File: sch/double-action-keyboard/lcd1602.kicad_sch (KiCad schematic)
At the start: 16 parts, among them U2 AQM1602XA-RN-GBW, U3 AQM1602Y-NLW-FBW

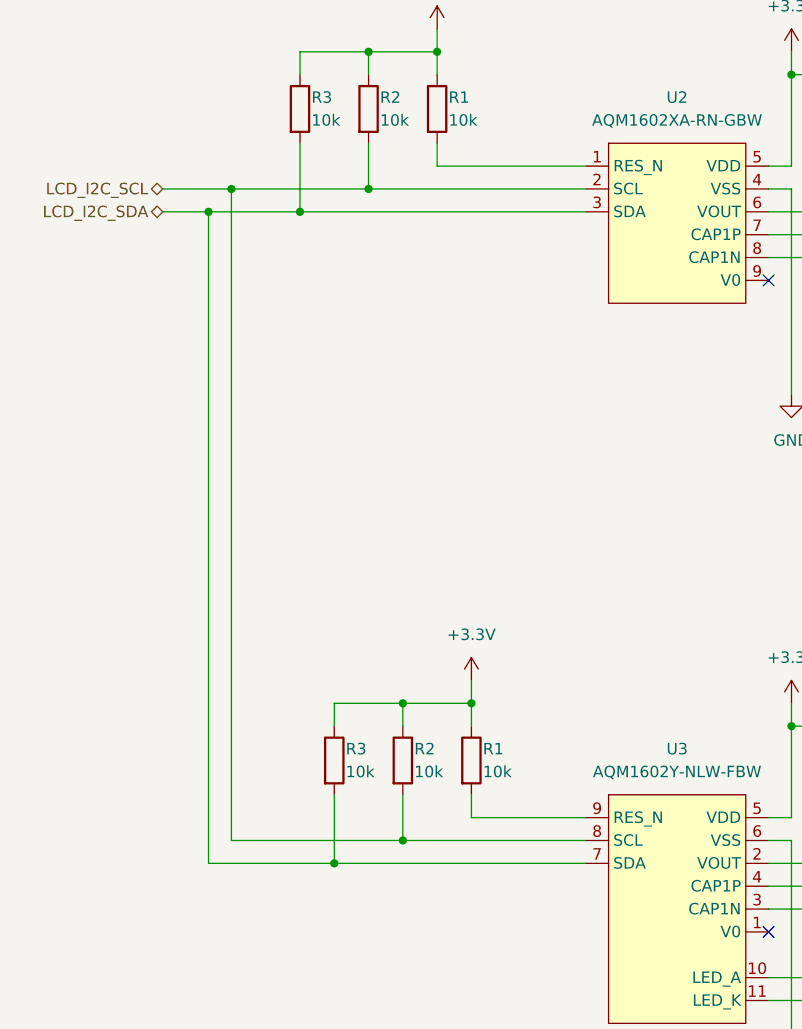
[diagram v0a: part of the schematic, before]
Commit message: ダイオードの配置と配線を行いました。
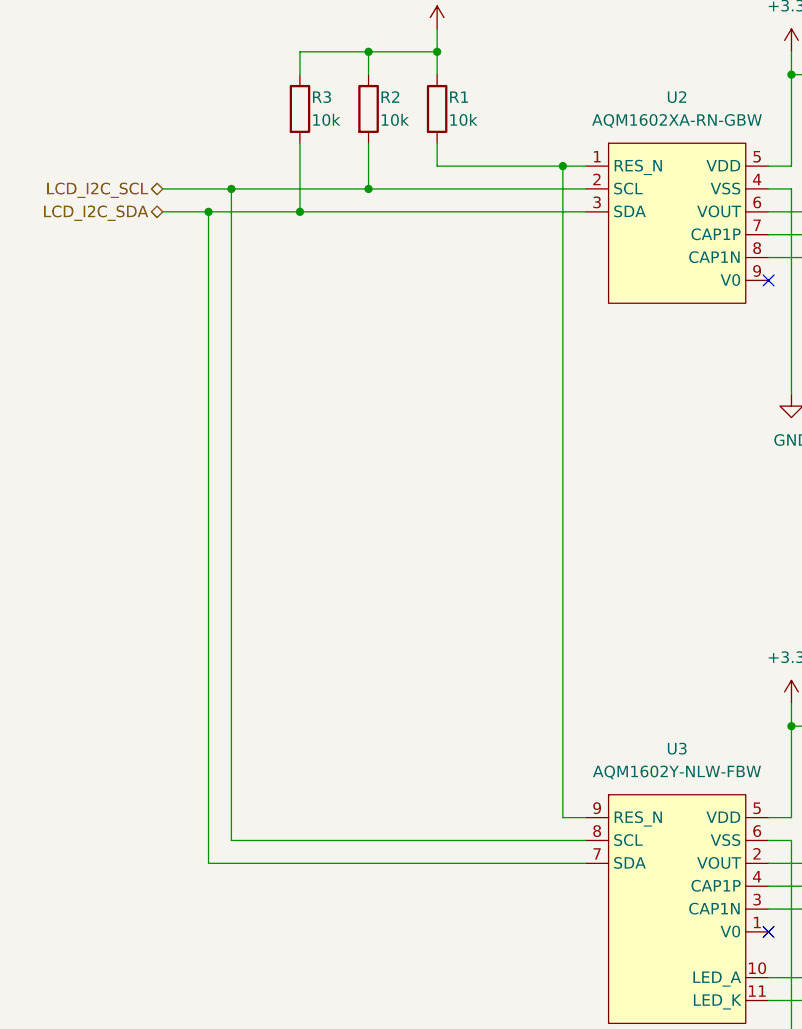
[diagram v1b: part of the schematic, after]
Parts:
- removed R1, R2, R3: 10k, Resistor_SMD:R_0603_1608Metric_Pad0.98x0.95mm_HandSolder, symbol Device:R
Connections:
- net at R1.2, U2.1 (RES_N): now also U3.9 (RES_N)

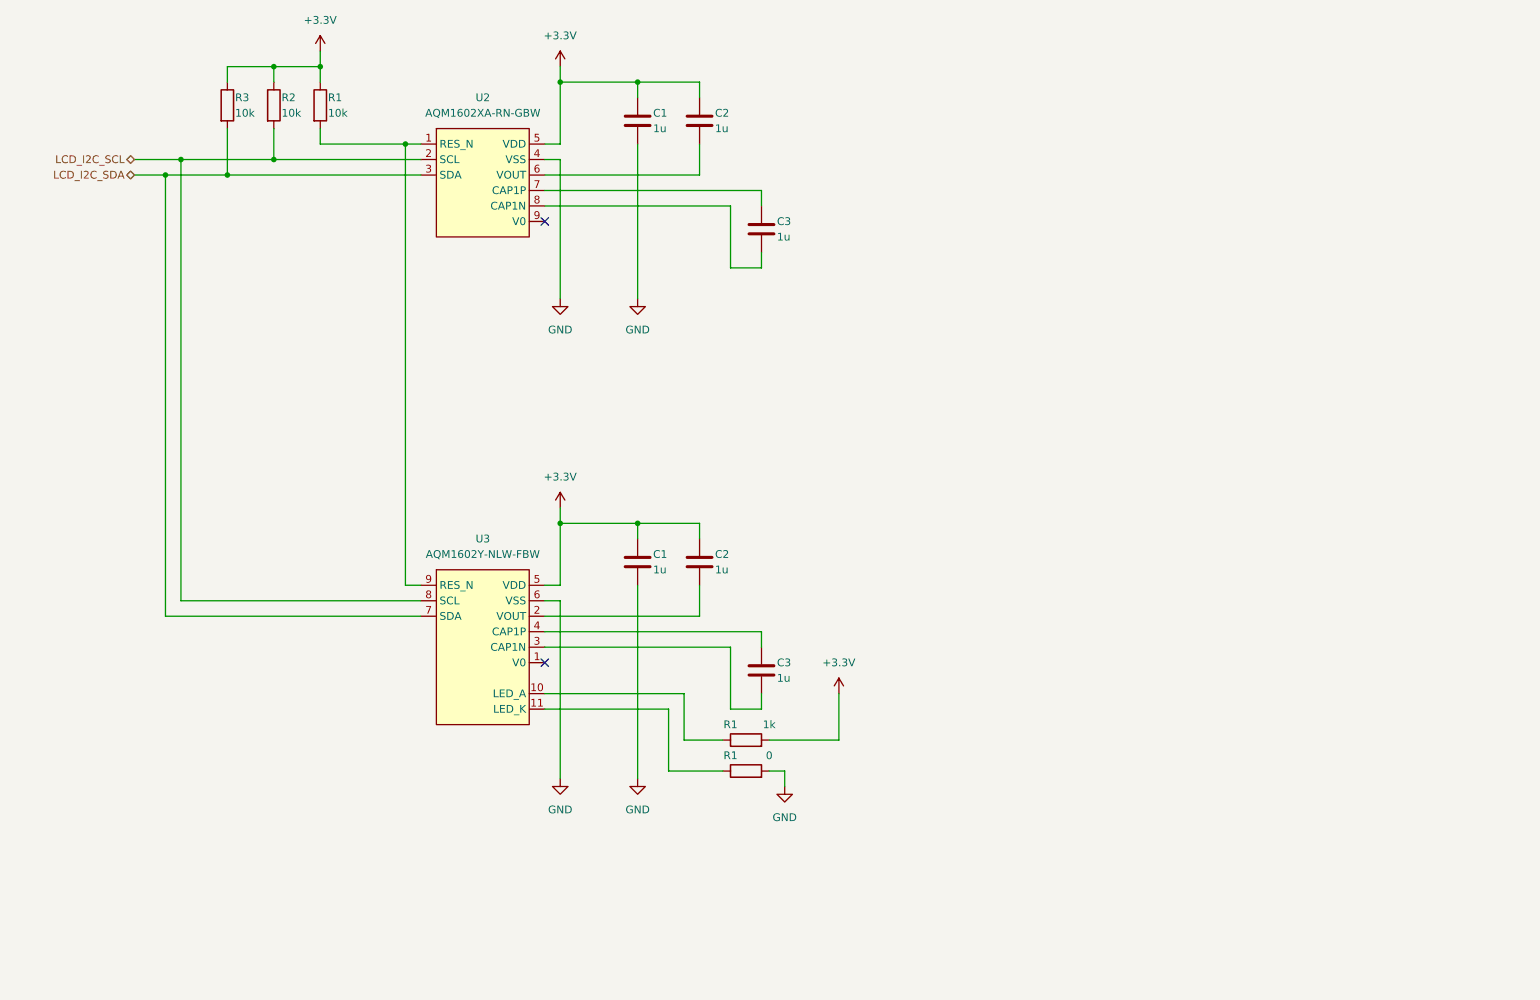
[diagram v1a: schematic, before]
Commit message: KiCad 8.0にアップデートしました。 部品配置をやり直し中。
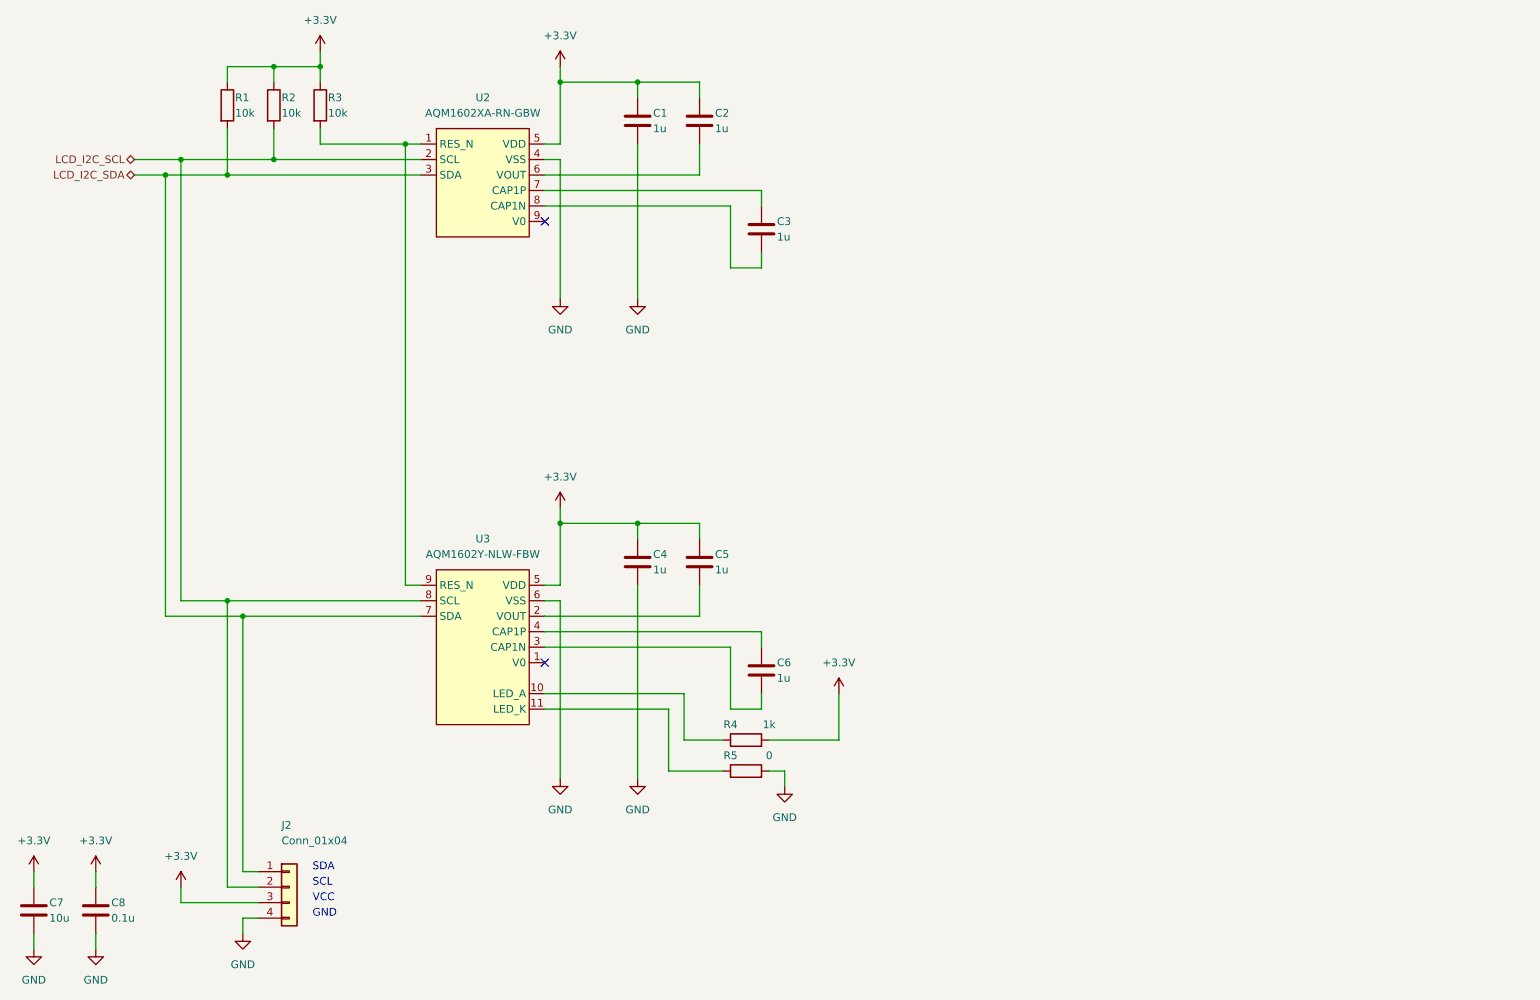
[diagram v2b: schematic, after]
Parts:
- added C7: 10u, Capacitor_SMD:C_0603_1608Metric_Pad1.08x0.95mm_HandSolder, symbol Device:C
- added C8: 0.1u, Capacitor_SMD:C_0603_1608Metric_Pad1.08x0.95mm_HandSolder, symbol Device:C
- added J2: Conn_01x04, Connector_PinHeader_2.54mm:PinHeader_1x04_P2.54mm_Vertical, symbol Connector_Generic:Conn_01x04
- renumbered C1 to C4, C2 to C5, C3 to C6, R3 to R1, R1 to R3, R1 to R4, R1 to R5
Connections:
- net +3.3V: now also C7.1, C8.1, J2.3 (Pin_3)
- net GND: now also C7.2, C8.2, J2.4 (Pin_4)
- net LCD_I2C_SCL: now also J2.2 (Pin_2)
- net LCD_I2C_SDA: now also J2.1 (Pin_1)
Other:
- note added: "GND"
- note added: "SCL"
- note added: "SDA"
- note added: "VCC"

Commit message: ざっくり配線しました。 線間はもっと詰める予定。
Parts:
- added C10: 0.1u, Capacitor_SMD:C_0603_1608Metric_Pad1.08x0.95mm_HandSolder, symbol Device:C
- added C9: 10u, Capacitor_SMD:C_0603_1608Metric_Pad1.08x0.95mm_HandSolder, symbol Device:C
- added J3: Conn_01x04, Connector_PinHeader_2.54mm:PinHeader_1x04_P2.54mm_Vertical, symbol Connector_Generic:Conn_01x04
- added R6: 10k, Resistor_SMD:R_0603_1608Metric_Pad0.98x0.95mm_HandSolder, symbol Device:R
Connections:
- net +3.3V: now also C10.1, C9.1, J3.3 (Pin_3), R6.1
- net GND: now also C10.2, C9.2, J3.4 (Pin_4)
- net LCD_I2C_SCL: now also J3.2 (Pin_2)
- net LCD_I2C_SDA: now also J3.1 (Pin_1)
- net at R3.2, U2.1 (RES_N): no longer U3.9 (RES_N)
- new net: R6.2, U3.9 (RES_N)
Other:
- note added: "OLED"
- moved on the sheet: C7, C8, J2

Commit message: ベタGNDにビアを打ちました。 空き領域にユニバーサル領域のスルーホールを追加しました。
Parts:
- J2, J3: footprint Connector_PinHeader_2.54mm:PinHeader_1x04_P2.54mm_Vertical -> OLED_I2C:OLED_I2C
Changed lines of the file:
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@@
 			)
 		)
-		(property "Footprint" "Connector_PinHeader_2.54mm:PinHeader_1x04_P2.54mm_Vertical"
+		(property "Footprint" "OLED_I2C:OLED_I2C"
 			(at 250.19 137.16 0)
 			(effects
@@
 			)
 		)
-		(property "Footprint" "Connector_PinHeader_2.54mm:PinHeader_1x04_P2.54mm_Vertical"
+		(property "Footprint" "OLED_I2C:OLED_I2C"
 			(at 250.19 100.33 0)
 			(effects
